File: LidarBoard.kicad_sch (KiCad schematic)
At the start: 46 parts, among them J19 ST-Link, J20 to TopBoard, J21 USB_C_Receptacle_USB2.0_16P, J22 LIDAR, J23 BNO055, J24 UNITV, J25 to TileBoard, J26 UNITV, J27 SERVO, J28 NeoPixel, Q6 BSS138, SW10 MODE_SWITCH, SW11 TC-06104-043E, SW12 TC-06104-043E, SW9 RESET_SWITCH, U19 RT9080-33GJ5, U20 CH340E, U21 STM32F446RET6, U22 Sit2001B

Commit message: メイン基板Rev.3
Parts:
- removed C49, C62: 4.7uF, Capacitor_SMD:C_0603_1608Metric, symbol Device:C
- removed C50, C51, C52, C53, C54, C55, C58, C59, C60, C61: 0.1uF, Capacitor_SMD:C_0603_1608Metric, symbol Device:C
- removed C56, C57: 1uF, Capacitor_SMD:C_0603_1608Metric, symbol Device:C
- removed C63: 15pF, Capacitor_SMD:C_0603_1608Metric, symbol Device:C
- removed D10: WS2812B, LED_SMD:LED_WS2812B_PLCC4_5.0x5.0mm_P3.2mm, symbol LED:WS2812B
- removed D8: LED, LED_SMD:LED_0603_1608Metric, symbol Device:LED
- removed J19: ST-Link, STDC14:CONN14_3220-14_CNC, symbol Connector:Conn_ST_STDC14
- removed J20: to TopBoard, Connector_PinHeader_2.54mm:PinHeader_1x04_P2.54mm_Vertical, symbol Connector:Conn_01x04_Socket
- removed J21: USB_C_Receptacle_USB2.0_16P, Connector_USB:USB_C_Receptacle_G-Switch_GT-USB-7010ASV, symbol Connector:USB_C_Receptacle_USB2.0_16P
- removed J22: LIDAR, Connector_JST:JST_PH_S4B-PH-K_1x04_P2.00mm_Horizontal, symbol Connector:Conn_01x04_Socket
- removed J23: BNO055, Connector_PinSocket_1.27mm:PinSocket_1x02_P1.27mm_Vertical, symbol Connector:Conn_01x02_Socket
- removed J24, J26: UNITV, Connector_PinSocket_1.27mm:PinSocket_1x02_P1.27mm_Vertical, symbol Connector:Conn_01x02_Socket
- removed J25: to TileBoard, Connector_PinSocket_1.27mm:PinSocket_1x02_P1.27mm_Vertical, symbol Connector:Conn_01x02_Socket
- removed J27: SERVO, Connector_PinSocket_1.27mm:PinSocket_1x02_P1.27mm_Vertical, symbol Connector:Conn_01x02_Socket
- removed J28: NeoPixel, Connector_PinSocket_1.27mm:PinSocket_1x02_P1.27mm_Vertical, symbol Connector:Conn_01x02_Socket
- removed Q6: BSS138, Package_TO_SOT_SMD:SOT-23, symbol Transistor_FET:BSS138
- removed R36, R37, R41, R42: 10k, Resistor_SMD:R_0603_1608Metric, symbol Device:R
- removed R38, R39: 5.1k, Resistor_SMD:R_0603_1608Metric, symbol Device:R
- removed R40: 470, Resistor_SMD:R_0603_1608Metric, symbol Device:R
- removed SW10: MODE_SWITCH, SSSS213202:SSSS213202, symbol Switch:SW_DPDT_x2
- removed SW11, SW12: TC-06104-043E, Button_Switch_SMD:SW_Push_1P1T_NO_6x6mm_H9.5mm, symbol Switch:SW_Push
- removed U19: RT9080-33GJ5, Package_TO_SOT_SMD:TSOT-23-5, symbol RT9080-33GJ5:RT9080-33GJ5
- removed U20: CH340E, Package_SO:MSOP-10_3x3mm_P0.5mm, symbol Interface_USB:CH340E
- removed U21: STM32F446RET6, Package_QFP:LQFP-64_10x10mm_P0.5mm, symbol MCU_ST_STM32F4:STM32F446RETx
- removed U22: Sit2001B, Package_TO_SOT_SMD:SOT-23-5, symbol SiT2001B:Sit2001B
- added C34, C46: 4.7uF, Capacitor_SMD:C_0603_1608Metric, symbol Device:C
- added C35, C36, C37, C38, C39, C40, C43, C44, C45: 0.1uF, Capacitor_SMD:C_0603_1608Metric, symbol Device:C
- added C41, C42: 1uF, Capacitor_SMD:C_0603_1608Metric, symbol Device:C
- added D10: LED, LED_SMD:LED_0603_1608Metric, symbol Device:LED
- added D12: WS2812B, LED_SMD:LED_WS2812B_PLCC4_5.0x5.0mm_P3.2mm, symbol LED:WS2812B
- added J15: ST-Link, STDC14:CONN14_3220-14_CNC, symbol Connector:Conn_ST_STDC14
- added J16: to TopBoard, Connector_JST:JST_XH_B4B-XH-A_1x04_P2.50mm_Vertical, symbol Connector:Conn_01x04_Socket
- added J17: USB_C_Receptacle_USB2.0_16P, Connector_USB:USB_C_Receptacle_G-Switch_GT-USB-7010ASV, symbol Connector:USB_C_Receptacle_USB2.0_16P
- added J18: LIDAR, Connector_JST:JST_PH_S4B-PH-K_1x04_P2.00mm_Horizontal, symbol Connector:Conn_01x04_Socket
- added R30: 470, Resistor_SMD:R_0603_1608Metric, symbol Device:R
- added R31, R32: 10k, Resistor_SMD:R_0603_1608Metric, symbol Device:R
- added R33, R34: 5.1k, Resistor_SMD:R_0603_1608Metric, symbol Device:R
- added SW10: TC-06104-043E, Button_Switch_SMD:SW_Push_1P1T_NO_6x6mm_H9.5mm, symbol Switch:SW_Push
- added SW7: RESET_SWITCH, SKRPACE010:SW_SKRPACE010, symbol Switch:SW_Push
- added SW8: MODE_SWITCH, SSSS213202:SSSS213202, symbol Switch:SW_DPDT_x2
- added U13: RT9080-33GJ5, Package_TO_SOT_SMD:TSOT-23-5, symbol RT9080-33GJ5:RT9080-33GJ5
- added U14: CH340E, Package_SO:MSOP-10_3x3mm_P0.5mm, symbol Interface_USB:CH340E
- added U15: STM32F446RET6, Package_QFP:LQFP-64_10x10mm_P0.5mm, symbol MCU_ST_STM32F4:STM32F446RETx
- added U16: AE-BNO055-BO, AE-BNO055-BO:AE-BNO055-BO, symbol AE-BNO055-BO:AE-BNO055-BO
- SW9: value RESET_SWITCH -> TC-06104-043E; footprint SKRPACE010:SW_SKRPACE010 -> Button_Switch_SMD:SW_Push_1P1T_NO_6x6mm_H9.5mm
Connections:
- net +3.3V: now also C34.1, C35.1, C36.1, C37.1, C38.1, C39.1, C40.1, C41.1, J15.3 (VCC), R31.1, U13.5 (VOUT), U15.1 (VBAT), U15.13 (VDDA), U15.19 (VDD), U15.32 (VDD), U15.48 (VDD), U15.64 (VDD), U16.1 (VCC)
- net +5V: now also C42.1, C44.1, D12.1 (VDD), J16.1 (Pin_1), J17.A4 (VBUS), J17.A9 (VBUS), J17.B4 (VBUS), J17.B9 (VBUS), J18.1 (Pin_1), R30.1, U13.1 (VIN), U13.3 (EN), U14.7 (VCC); no longer R35.1
- net GND: now also C34.2, C35.2, C36.2, C37.2, C38.2, C39.2, C40.2, C41.2, C42.2, C43.1, C44.2, C45.1, C46.2, D10.1 (K), D12.3 (VSS), J15.11 (GNDDetect), J15.5 (GND), J15.7 (GND), J16.2 (Pin_2), J17.A1 (GND), J17.A12 (GND), J17.B1 (GND), J17.B12 (GND), J18.3 (Pin_3), R32.1, R33.2, R34.2, SW10.1, SW7.1, U13.2 (GND), U14.3 (GND), U15.12 (VSSA), U15.18 (VSS), U15.31 (VSS), U15.47 (VSS), U15.63 (VSS), U16.2 (GND)
- net IN: now also D11.4 (DIN), U15.61 (PB8)
- net NRST: now also C43.2, J15.12 (~{RST}), SW7.2, U15.7 (NRST); no longer SW9.2
- net RX1: now also J15.13 (VCP_RX), U15.43 (PA10)
- net RX2: now also J18.2 (Pin_2), U15.17 (PA3)
- net RX3: now also J16.4 (Pin_4), U15.25 (PC5)
- net RX4: now also U14.8 (TXD), U15.15 (PA1)
- net SCL: now also U15.58 (PB6), U16.4 (SCL/R)
- net SDA: now also U15.59 (PB7), U16.3 (SDA/T)
- net SWCLK: now also J15.6 (JCLK/SWCLK), U15.49 (PA14)
- net SWDIO: now also J15.4 (JTMS/SWDIO), U15.46 (PA13)
- net SWO: now also J15.8 (JTDO/SWO), U15.55 (PB3)
- net TX1: now also J15.14 (VCP_TX), U15.42 (PA9)
- net TX2: now also J18.4 (Pin_4), U15.16 (PA2)
- net TX3: now also J16.3 (Pin_3), U15.29 (PB10)
- net TX4: now also U14.9 (RXD), U15.14 (PA0)
- net at D9.2 (A): now also R30.2
- net at R35.2: now also U14.6 (TNOW)
- net at D11.2 (DOUT): now also D12.4 (DIN)
- new net: C45.2, U14.10 (V3)
- new net: R32.2, SW8.3 (C)
- new net: SW9.2, U15.33 (PB12)
- new net: J17.B5 (CC2), R34.1
- new net: C46.1, U15.30 (VCAP_1)
- new net: R31.2, SW8.1 (A)
- new net: J17.A6 (D+), J17.B6 (D+), U14.1 (UD+)
- new net: J17.A7 (D-), J17.B7 (D-), U14.2 (UD-)
- new net: U14.4 (~{RTS}), U14.5 (~{CTS})
- new net: SW8.2 (B), U15.60 (BOOT0)
- new net: SW10.2, U15.34 (PB13)
- new net: D10.2 (A), R35.1
- new net: J17.A5 (CC1), R33.1
- no-connect marks 30 -> 44
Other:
- note added: "IMU"
- note added: "LED"
- note added: "LiDAR"
- note added: "MainMCU"
- note added: "Power&Com"
- note added: "USB_Power&Com"
- note added: "XH,Vertical"
- note removed: "CONN"
- note removed: "LIDAR"
- note removed: "NEOPIXEL"
- note removed: "POWER&COM"
- note removed: "PinHeader,Vertical"
- note removed: "STM32"
- note removed: "USB_POWER&COM"
- company: Fornax -> (none)
- title: LidarBoard Rev.2 -> LiDAR_Board_Rev.3

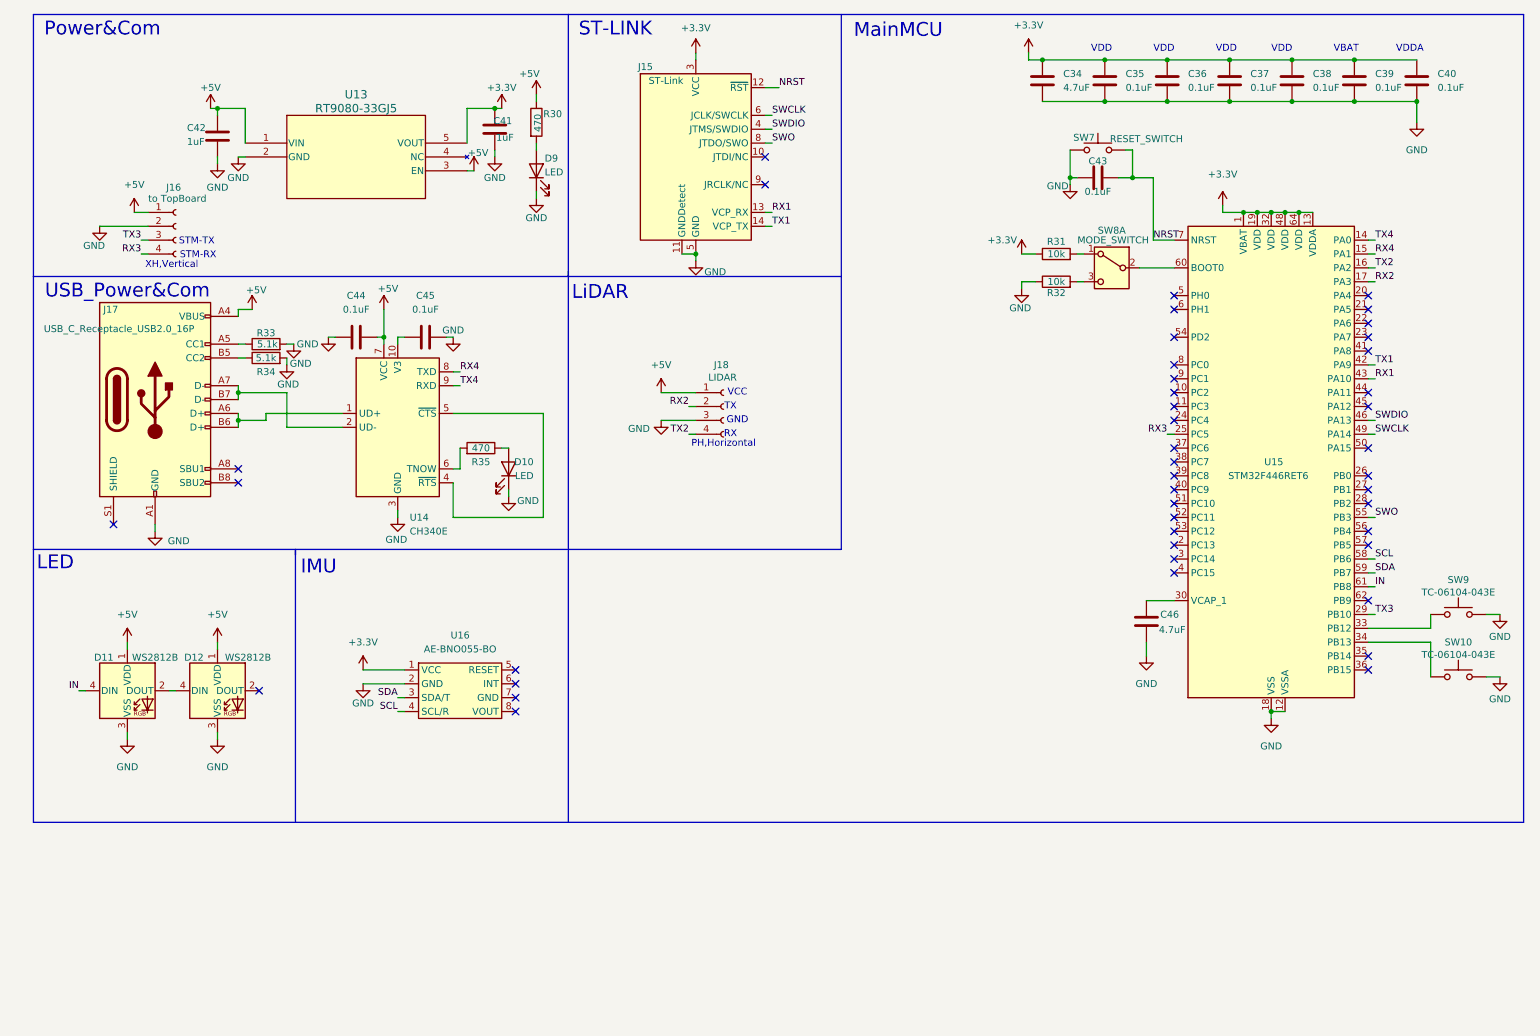
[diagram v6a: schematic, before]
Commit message: LiDAR基板Rev.3コネクタ配置
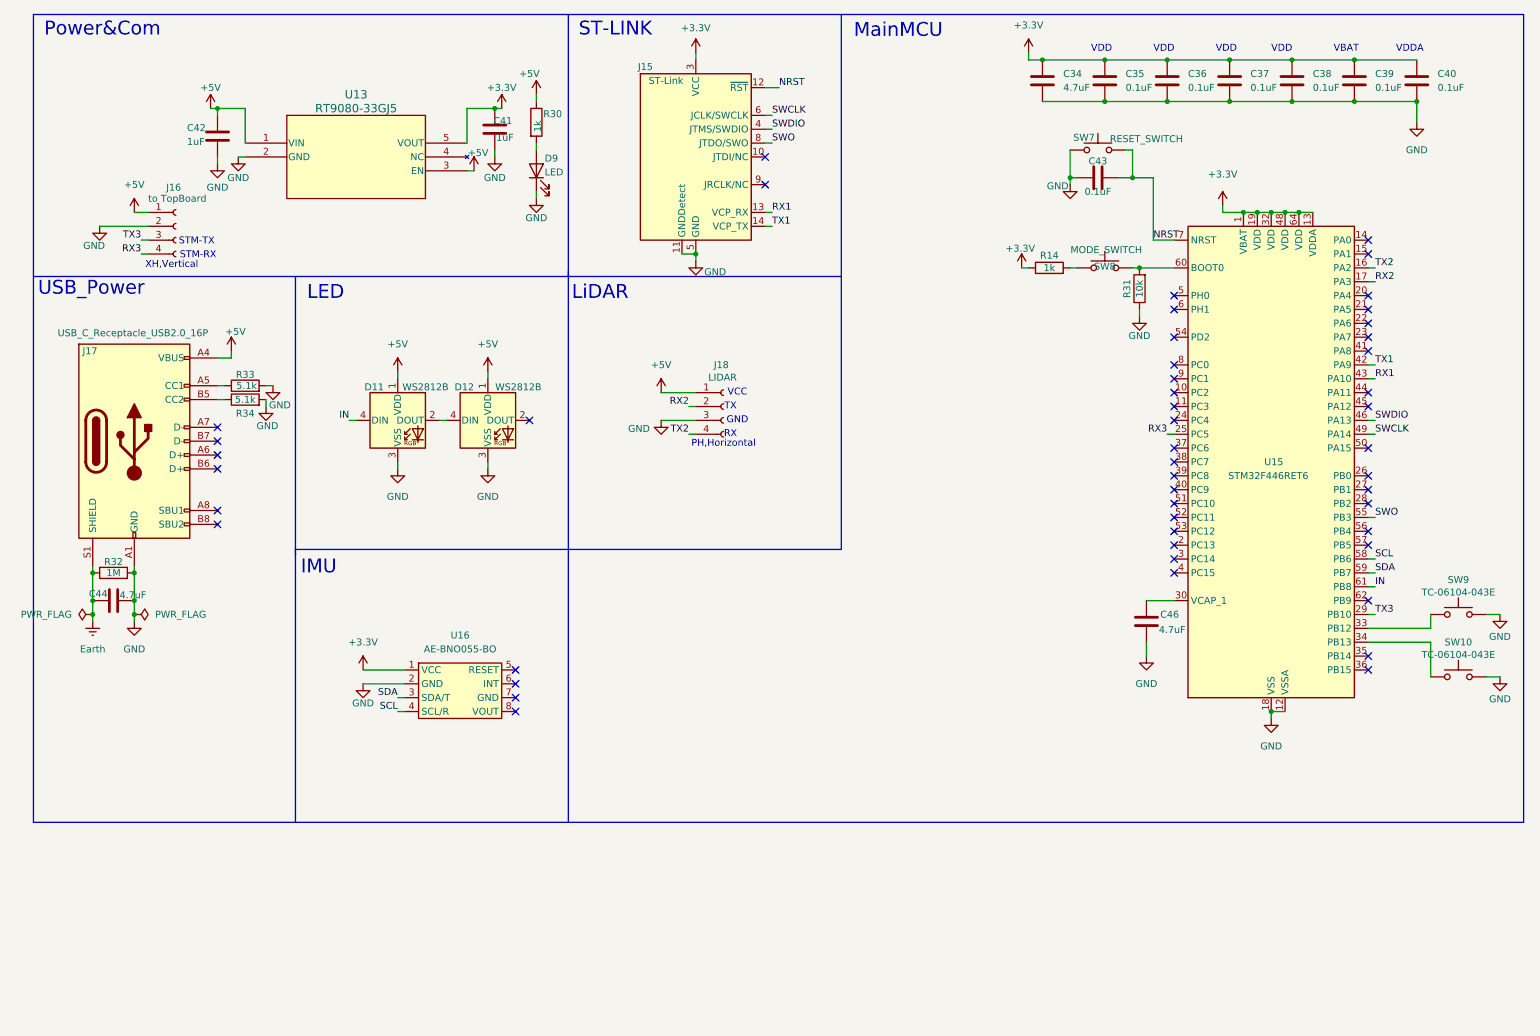
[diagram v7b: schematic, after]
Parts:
- removed C45: 0.1uF, Capacitor_SMD:C_0603_1608Metric, symbol Device:C
- removed D10: LED, LED_SMD:LED_0603_1608Metric, symbol Device:LED
- removed R35: 470, Resistor_SMD:R_0603_1608Metric, symbol Device:R
- removed SW8: MODE_SWITCH, SSSS213202:SSSS213202, symbol Switch:SW_DPDT_x2
- removed U14: CH340E, Package_SO:MSOP-10_3x3mm_P0.5mm, symbol Interface_USB:CH340E
- added R14: 1k, Resistor_SMD:R_0603_1608Metric_Pad0.98x0.95mm_HandSolder, symbol Device:R
- added SW8: MODE_SWITCH, SKRPACE010:SW_SKRPACE010, symbol Switch:SW_Push
- C44: value 0.1uF -> 4.7uF
- R30: value 470 -> 1k
- R31: footprint Resistor_SMD:R_0603_1608Metric -> Resistor_SMD:R_0603_1608Metric_Pad0.98x0.95mm_HandSolder
- R32: value 10k -> 1M
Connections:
- net +3.3V: now also R14.1; no longer R31.1
- net +5V: no longer C44.1
- net GND: now also R31.1, R32.2; no longer R32.1
- net at R31.2: now also U15.60 (BOOT0), SW8.2
- net at J17.A6 (D+): no longer J17.B6 (D+)
- net at J17.A7 (D-): no longer J17.B7 (D-)
- net Earth: now reaches J17.S1 (SHIELD)
- net Earth: now also C44.1, R32.1
- net RX4: no longer names the net of U15.15 (PA1)
- net TX4: no longer names the net of U15.14 (PA0)
- new net: R14.2, SW8.1
- no-connect marks 44 -> 49
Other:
- note added: "USB_Power"
- note removed: "USB_Power&Com"
- moved on the sheet: D11, D12, J17, R33, R34

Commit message: メイン基板Rev.3
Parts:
- removed SW10, SW9: TC-06104-043E, Button_Switch_SMD:SW_Push_1P1T_NO_6x6mm_H9.5mm, symbol Switch:SW_Push
- added D12, D13: WS2812B, LED_SMD:LED_WS2812B_PLCC4_5.0x5.0mm_P3.2mm, symbol LED:WS2812B
- C51: renamed from C43; footprint Capacitor_SMD:C_0603_1608Metric -> Capacitor_SMD:C_0603_1608Metric_Pad1.08x0.95mm_HandSolder
- renumbered C34 to C42, C35 to C43, C36 to C44, C37 to C45, C38 to C46, C39 to C47, C40 to C48, C41 to C49, C42 to C50, C44 to C52, C46 to C53, D11 to D10, D12 to D11, J15 to J16, J16 to J17, J17 to J18, J18 to J19, R30 to R29, R14 to R30, R33 to R32, R34 to R33, R32 to R34, U15 to U14, U16 to U15
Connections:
- net +5V: now also D12.1 (VDD), D13.1 (VDD)
- net GND: now also D12.3 (VSS), D13.3 (VSS)
- net at D11.2 (DOUT): now also D12.4 (DIN)
- net SWO: no longer names the net of J16.8 (JTDO/SWO)
- net SWO: no longer U14.55 (PB3)
- new net: D12.2 (DOUT), D13.4 (DIN)
- no-connect marks 49 -> 53
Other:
- moved on the sheet: D10, D11, J19
